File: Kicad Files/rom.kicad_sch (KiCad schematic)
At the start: 20 parts, among them U13 HM62256BLP, U14 74LS245

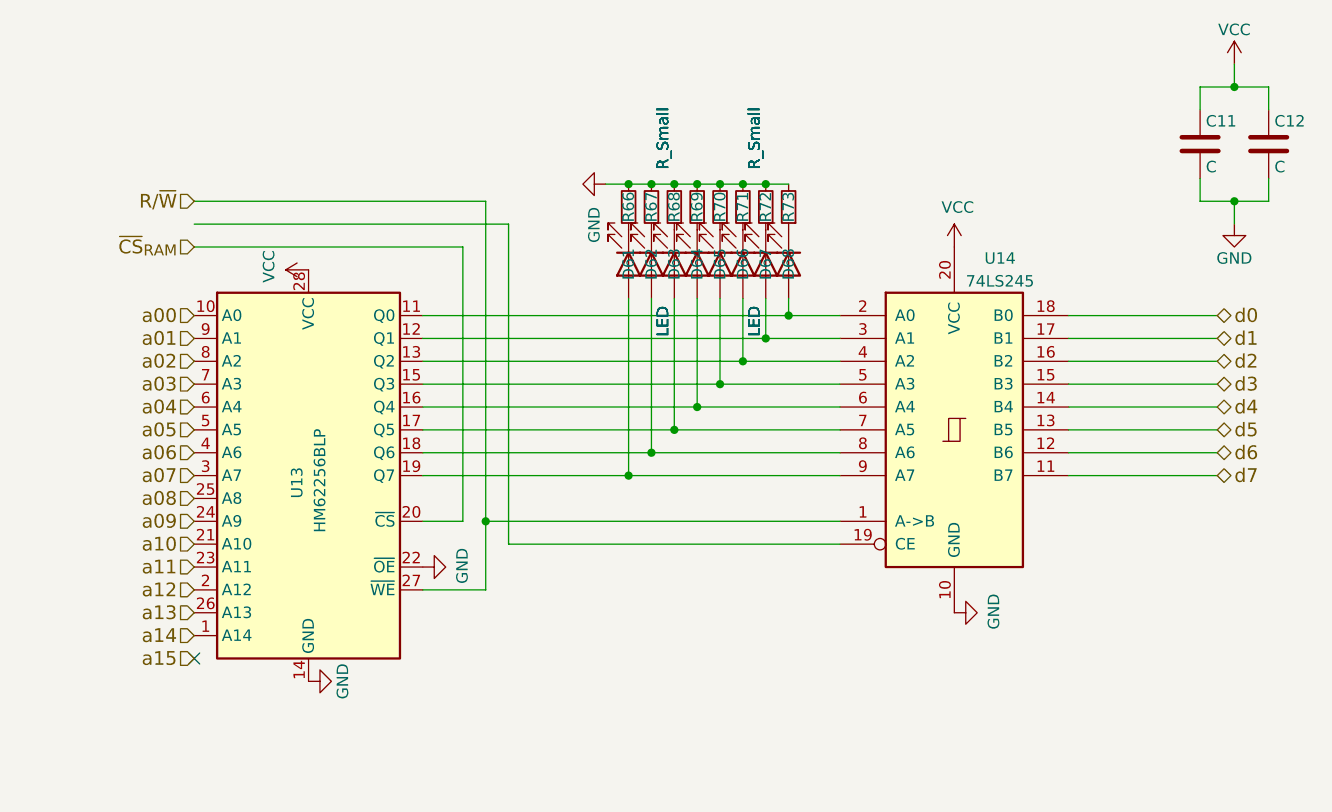
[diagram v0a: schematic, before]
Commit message: complete redraw to bus system
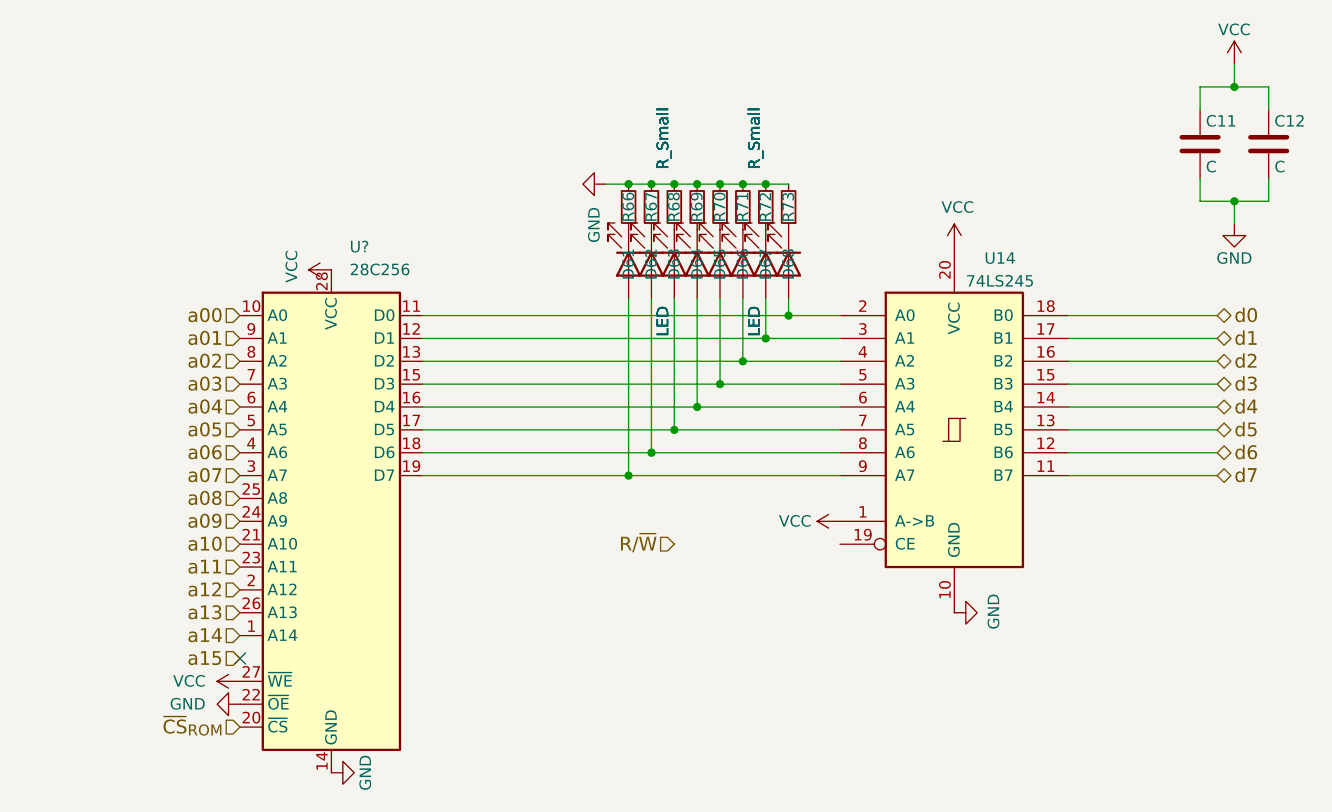
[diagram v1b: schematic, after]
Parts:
- removed U13: HM62256BLP, Package_DIP:DIP-28_W15.24mm, symbol Memory_RAM:HM62256BLP
- added U?: 28C256, symbol Memory_EEPROM:28C256
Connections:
- net GND: now also U?.14 (GND), U?.22 (~{OE})
- net R/~{W}: no longer U14.1 (A->B)
- net VCC: now also U14.1 (A->B), U?.27 (~{WE}), U?.28 (VCC)
- net a00: now also U?.10 (A0)
- net a01: now also U?.9 (A1)
- net a02: now also U?.8 (A2)
- net a03: now also U?.7 (A3)
- net a04: now also U?.6 (A4)
- net a05: now also U?.5 (A5)
- net a06: now also U?.4 (A6)
- net a07: now also U?.3 (A7)
- net a08: now also U?.25 (A8)
- net a09: now also U?.24 (A9)
- net a10: now also U?.21 (A10)
- net a11: now also U?.23 (A11)
- net a12: now also U?.2 (A12)
- net a13: now also U?.26 (A13)
- net a14: now also U?.1 (A14)
- net at D68.2 (A), U14.2 (A0): now also U?.11 (D0)
- net at D67.2 (A), U14.3 (A1): now also U?.12 (D1)
- net at D66.2 (A), U14.4 (A2): now also U?.13 (D2)
- net at D65.2 (A), U14.5 (A3): now also U?.15 (D3)
- net at D64.2 (A), U14.6 (A4): now also U?.16 (D4)
- net at D63.2 (A), U14.7 (A5): now also U?.17 (D5)
- net at D62.2 (A), U14.8 (A6): now also U?.18 (D6)
- net at D61.2 (A), U14.9 (A7): now also U?.19 (D7)
- new net ~{CS}_{ROM}: U?.20 (~{CS})

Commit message: update
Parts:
- removed C11, C12: C, Capacitor_THT:C_Disc_D4.3mm_W1.9mm_P5.00mm, symbol Device:C
- removed D61, D62, D63, D64, D65, D66, D67, D68: LED, symbol Device:LED
- removed R66, R67, R68, R69, R70, R71, R72, R73: R_Small, symbol Device:R_Small
- removed U14: 74LS245, symbol 74xx:74LS245
- added D9: LED_Small, symbol Device:LED_Small
- added R9: R_Small, symbol Device:R_Small
- gave numbers to parts that had none: 1
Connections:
- net GND: no longer U1.22 (~{OE})
- net VCC: now also R9.2
- net ~{CS}_{ROM}: now also D9.1 (K)
- net d_{e}0: now reaches U1.11 (D0)
- net d_{e}1: now reaches U1.12 (D1)
- net d_{e}2: now reaches U1.13 (D2)
- net d_{e}3: now reaches U1.15 (D3)
- net d_{e}4: now reaches U1.16 (D4)
- net d_{e}5: now reaches U1.17 (D5)
- net d_{e}6: now reaches U1.18 (D6)
- net d_{e}7: now reaches U1.19 (D7)
- new net: D9.2 (A), R9.1
- new net ~{R}/W: U1.22 (~{OE})
- no-connect marks 1 -> 0
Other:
- moved on the sheet: U1
